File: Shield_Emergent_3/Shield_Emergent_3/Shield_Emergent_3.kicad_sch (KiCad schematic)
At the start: 29 parts, among them J1 USB3_B_Micro, J2 Conn_01x04_Socket, J3 USB3_B_Micro, J4 Conn_01x05, J5 Conn_01x02_Socket, J6 Conn_01x02_Socket, J7 Conn_01x05, J9 Conn_01x10, U3 SP3012-06UTG, U4 SP3012-06UTG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

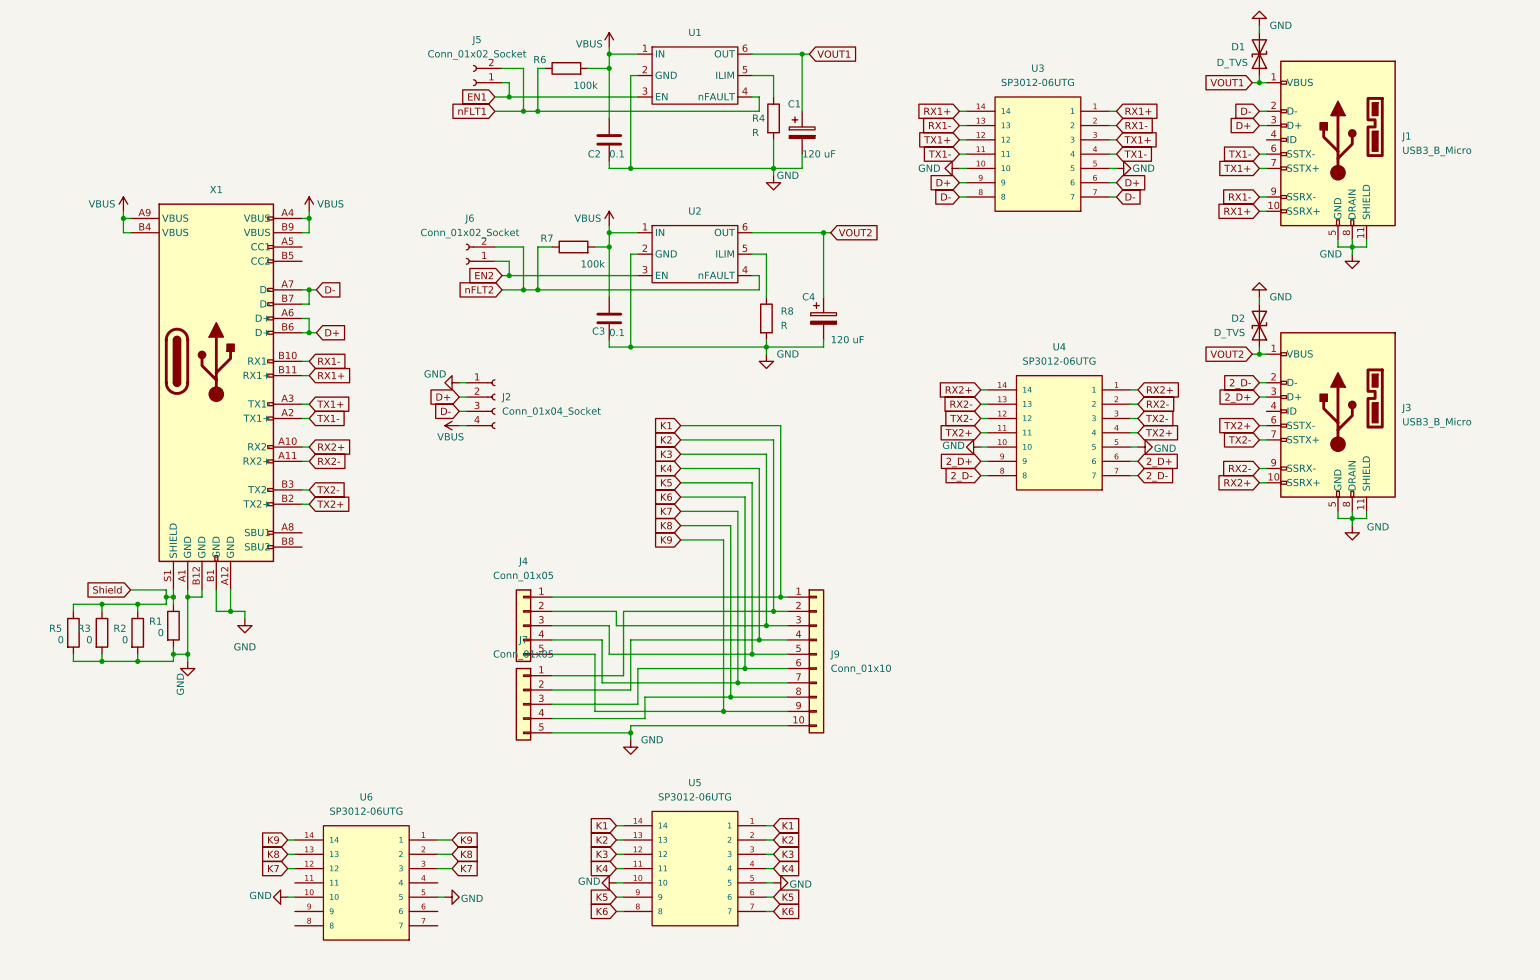
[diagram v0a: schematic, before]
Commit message: v2.1 prothos 4 15-pin connector
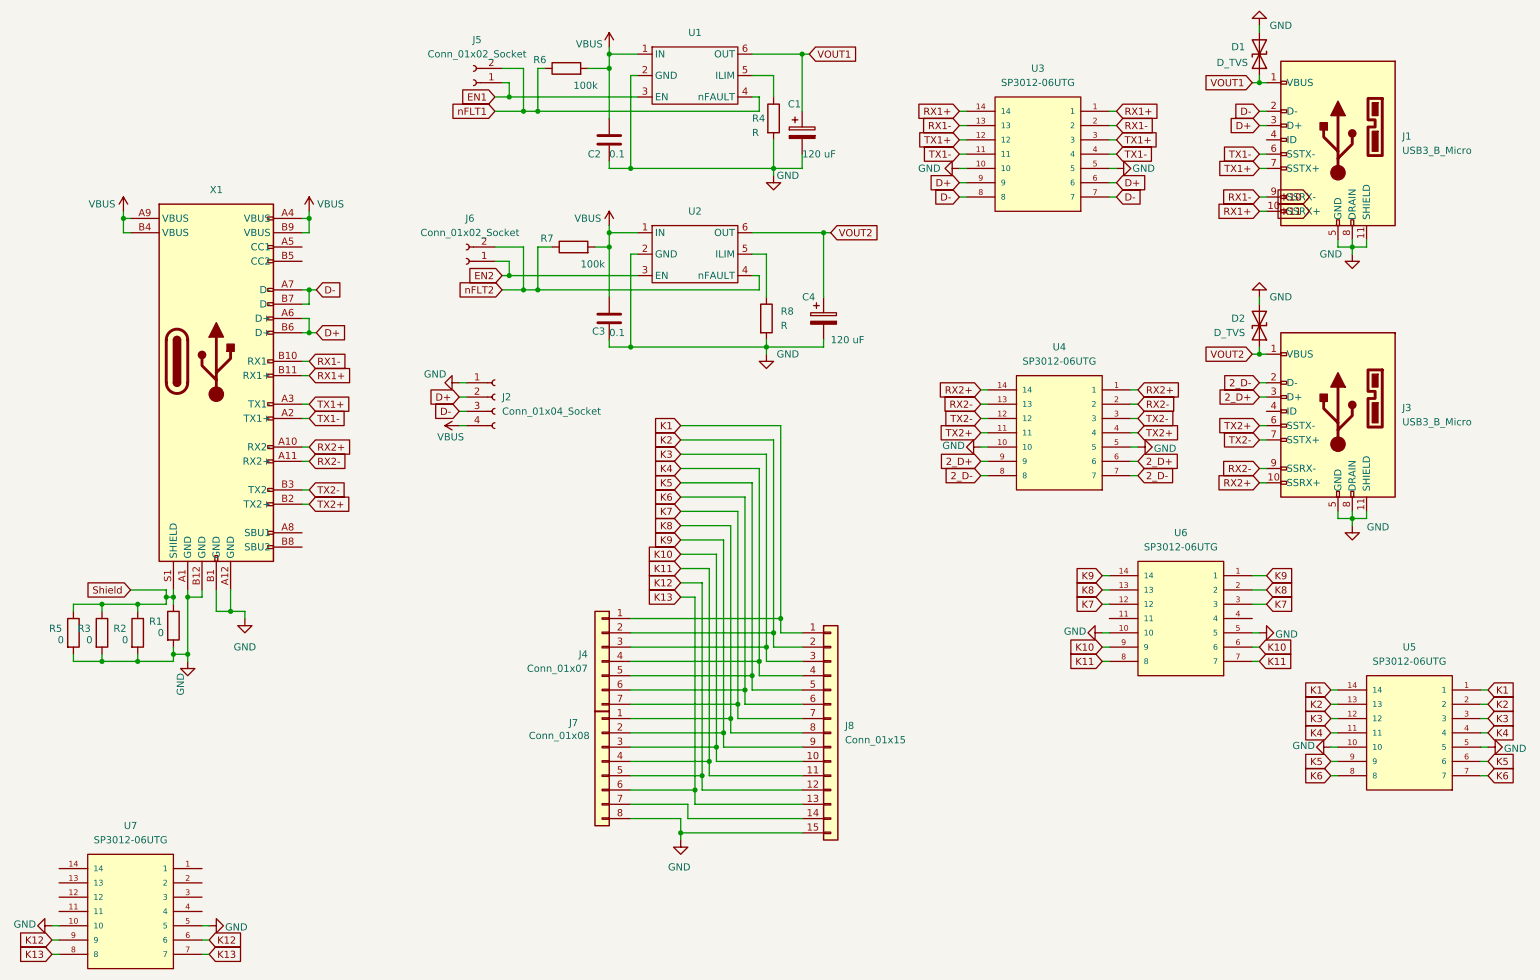
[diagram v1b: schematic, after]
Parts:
- removed J4, J7: Conn_01x05, Connector_PinHeader_1.27mm:PinHeader_1x05_P1.27mm_Vertical, symbol Connector_Generic:Conn_01x05
- removed J9: Conn_01x10, Connector_PinHeader_1.00mm:PinHeader_1x10_P1.00mm_Vertical_SMD_Pin1Left, symbol Connector_Generic:Conn_01x10
- added J4: Conn_01x07, Connector_PinHeader_1.27mm:PinHeader_1x04_P1.27mm_Vertical, symbol Connector_Generic:Conn_01x07
- added J7: Conn_01x08, Connector_PinHeader_1.27mm:PinHeader_1x08_P1.27mm_Vertical, symbol Connector_Generic:Conn_01x08
- added J8: Conn_01x15, symbol Connector_Generic:Conn_01x15
- added U7: SP3012-06UTG, myLib8:DFN-14_1.35x3.5mm_P0.5mm, symbol myLib8:SP3012-06UTG
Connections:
- net GND: now also J7.8 (Pin_8), J8.15 (Pin_15), U7.10, U7.5
- net K1: now also J4.1 (Pin_1), J8.1 (Pin_1)
- net K2: now also J4.2 (Pin_2), J8.2 (Pin_2)
- net K3: now also J4.3 (Pin_3), J8.3 (Pin_3)
- net K4: now also J4.4 (Pin_4), J8.4 (Pin_4)
- net K5: now also J4.5 (Pin_5), J8.5 (Pin_5)
- net K6: now also J4.6 (Pin_6), J8.6 (Pin_6)
- net K7: now also J4.7 (Pin_7), J8.7 (Pin_7)
- net K8: now also J7.1 (Pin_1), J8.8 (Pin_8)
- net K9: now also J7.2 (Pin_2), J8.9 (Pin_9)
- net K10: now reaches U6.6
- net K10: now also U6.9, J7.3 (Pin_3), J8.10 (Pin_10)
- net K11: now reaches U6.7
- net K11: now also U6.8, J7.4 (Pin_4), J8.11 (Pin_11)
- new net: J7.7 (Pin_7), J8.14 (Pin_14)
- new net K12: J7.5 (Pin_5), J8.12 (Pin_12), U7.6, U7.9
- new net K13: J7.6 (Pin_6), J8.13 (Pin_13), U7.7, U7.8
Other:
- moved on the sheet: U5, U6
